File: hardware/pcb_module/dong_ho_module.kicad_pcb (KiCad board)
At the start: 2 copper layers, 50 x 62 mm, 36 parts, among them J1 Motor rung 1027, J2 Pogo sạc (cái, nam châm), J3 Pin LiPo 603040 (JST PH2.0), J4 Dây sang BAT+/BAT- của XIAO, J5 Nút SOS, J6 Dây RA -> vít thép mép vỏ, Q1 AO3400A, U1 XIAO nRF52840 Sense, U2 MAX30102 (module tím), U3 CJMCU-30205, U4 AD8232 (module), U5 GC9A01 1.28in

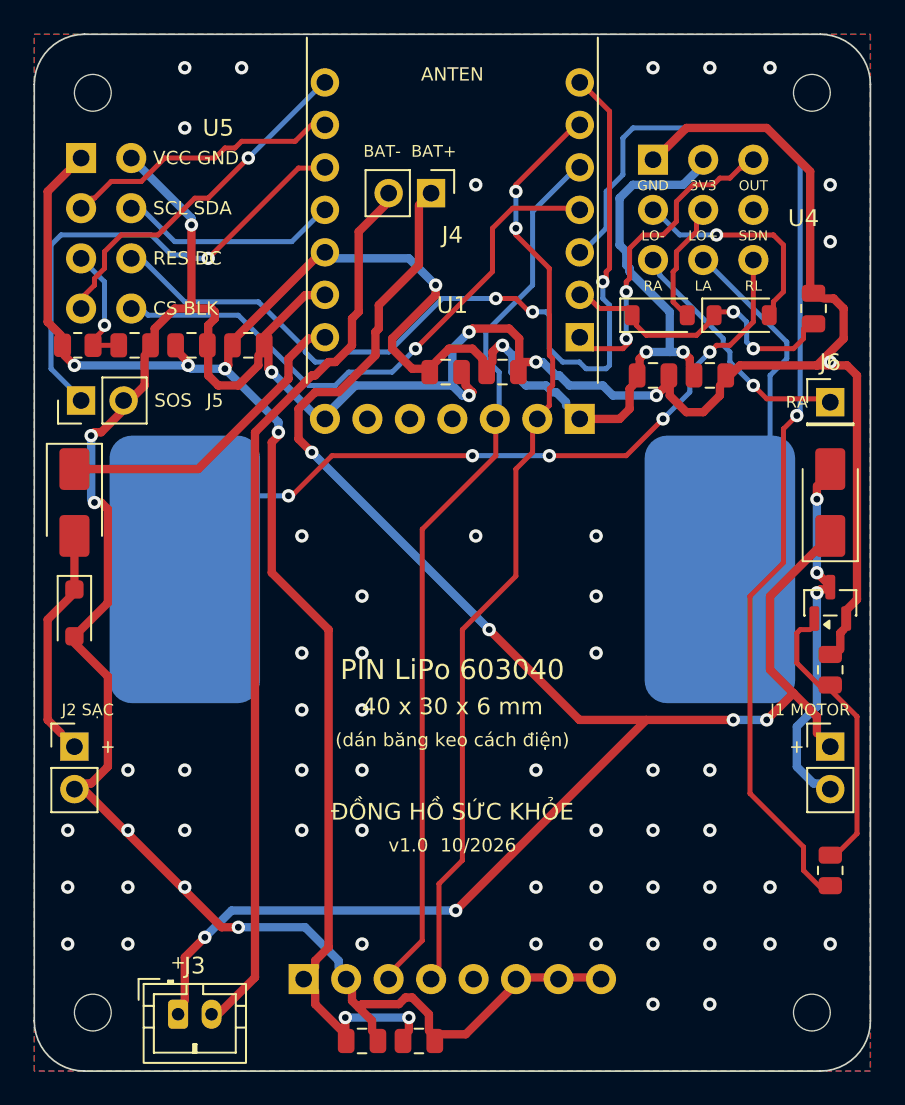
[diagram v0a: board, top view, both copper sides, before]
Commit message: PCB module 1.1: dựng lại bằng KiCad 10 với MAX30102 2x4
- Chạy lại gen_fp/gen_sch/gen_pcb trên KiCad 10.0.7, thêm footprint Module_MAX30102_2x4.
- U2 đổi góc 180 -> 0 (vẫn lật mặt dưới) để chân khớp module thật:
  VIN (28,81; 24,92) ... INT (21,19; 35,08).
- D4 (TVS SMA) dời xuống y 35,4 để courtyard không chồng D5.
- Chữ chân U2 trên lụa 0,6/0,1 mm cho đúng quy tắc lụa.
- ERC 0 lỗi 0 cảnh báo; DRC 0 vi phạm, 0 chưa nối, khớp sơ đồ 0 lỗi.
- Xuất lại PDF, BOM, gerber + khoan, zip và ảnh 3D hai mặt.

Co-Authored-By: Claude Opus 5.5 <noreply@anthropic.com>
Claude-Session: https://claude.ai/code/session_016xjgaR8Q12uTCt4QMw8J44
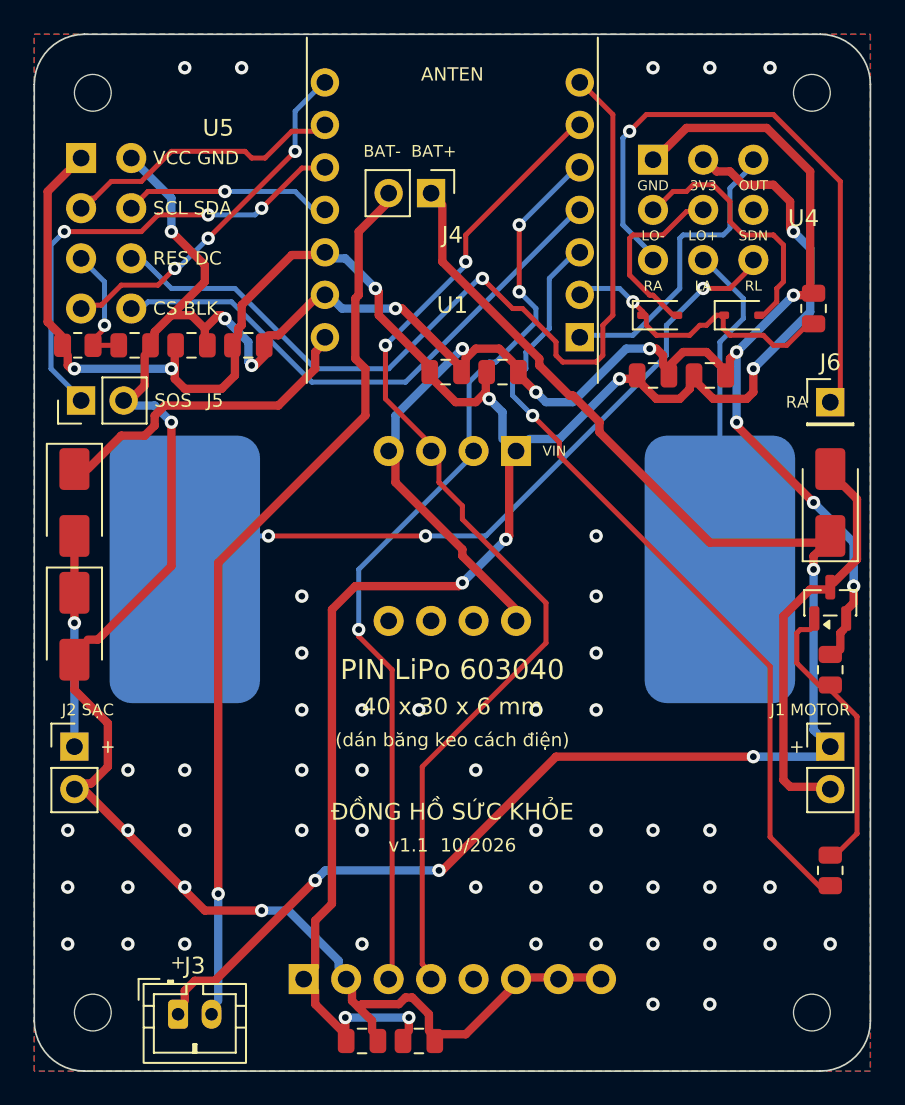
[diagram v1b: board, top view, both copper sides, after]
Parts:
- D2, D3: value 1N4148W -> 1N4148WS; footprint Diode_SMD:D_SOD-123 -> Diode_SMD:D_SOD-323
- D4: value SMF5.0A -> SMAJ5.0A; footprint Diode_SMD:D_SOD-123F -> Diode_SMD:D_SMA
- U2: value MAX30102 (module tím) -> MAX30102 (module 2x4); footprint DoAnModule:Module_MAX30102_1x7 -> DoAnModule:Module_MAX30102_2x4
- moved U2 10.3 mm to (125.0, 130.0), turned to 0 degrees
- moved D4 0.80 mm to (102.4, 135.4)
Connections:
- U2 pad 2: /I2C_SCL -> /I2C_SDA
- U2 pad 3: /I2C_SDA -> /I2C_SCL
- U2 pad 4: unconnected-(U2-INT-Pad4) -> GND
- U2 pad 5: unconnected-(U2-IRD-Pad5) -> GND
- U2 pad 7: GND -> unconnected-(U2-IRD-Pad7)
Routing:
- net /ECG_RA: track 13.3 -> 35.0 mm
- net /MOTOR_EN: track 65.3 -> 46.6 mm
- net /VBAT+: track 104.4 -> 88.5 mm, vias 6 -> 4
- net /I2C_SCL: track 53.3 -> 59.9 mm
- net GND: track 173.3 -> 179.6 mm, vias 63 -> 64
- net +3V3: track 125.0 -> 129.0 mm, vias 10 -> 11
- net /LO_P: track 6.23 -> 10.1 mm
- net /MOTOR_N: track 19.4 -> 22.1 mm, vias 3 -> 0
- net /LO_N: track 11.9 -> 14.5 mm, vias 1 -> 0
- net /VCHG: track 10.9 -> 8.40 mm, vias 0 -> 1
- net /I2C_SDA: track 50.7 -> 53.0 mm, vias 0 -> 3
- net /TFT_BLK: track 33.1 -> 31.5 mm, vias 1 -> 0
- net /ECG_OUT: track 17.6 -> 16.4 mm, vias 2 -> 0
- net /SOS_BTN: track 27.8 -> 26.6 mm, vias 1 -> 3
- net /ECG_LOD: track 15.1 -> 16.2 mm, vias 2 -> 1
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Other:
- board text added: "VIN"
- board text added: "v1.1 10/2026"
- board text removed: "v1.0 10/2026"

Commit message: PCB 1.2: áp tiêu chuẩn xưởng, DRC 0 lỗi, xuất lại Gerber
- Chạy cong_cu/ap_quy_tac_xuong.py trên KiCad 10.0.7: 58 pad xuyên lỗ, 101 via,
  2 vùng phủ GND, 50 chữ lụa, 106 nét lụa.
- Lỗ khoan PTH chỉ còn 0,3 (via), 0,8 (JST) và 1,0 mm (header), pad = lỗ + 0,6 mm;
  via 0,3 / 0,9 mm trên cả F.Cu và B.Cu; phủ đồng GND cách 0,65 mm, thermal 0,5 mm.
  Lỗ bắt vít H1-H4 giữ 2,2 mm không mạ.
- Sửa script: làm tròn khi đổi mm (0,3 + 0,6 bị cắt còn 0,899999 mm làm DRC báo
  202 lỗi via) và đặt cỡ via theo từng lớp (API KiCad 10, hết hộp Debug Alert).
- Dời chữ lụa "RA" cạnh J6 sang trái 0,6 mm cho khỏi chồng viền J6.
- ERC 0 lỗi 0 cảnh báo; DRC 0 lỗi, 0 chưa nối, khớp sơ đồ 0 lỗi; còn 6 cảnh báo
  lib_footprint_mismatch J1-J6 (cố ý nới pad).
- Xuất lại PDF, gerber + khoan, zip và ảnh 3D hai mặt; README ghi lệnh xuất đủ lớp.

Co-Authored-By: Claude Opus 5.5 <noreply@anthropic.com>
Claude-Session: https://claude.ai/code/session_01DtVKYLjz9b4xdEphcSQTzb
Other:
- board text added: "v1.2 10/2026"
- board text removed: "v1.1 10/2026"

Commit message: PCB 1.3: vùng pin 45 mm, chuyển D1/Q1/R1/R2 xuống mặt dưới
- Pin thật đo được 45 x 30 x 5,5 mm (tính cả mạch bảo vệ), dài hơn vùng 40 mm của bản 1.2.
  Vùng pin mặt trên nới tới mép phải (x 5-50 mm); khung pin trên User.Comments/F.Fab và
  chữ lụa đổi thành 45 x 30 x 5.5 mm (PCM ->), nhãn v1.3.
- D1 (SS14), Q1 (AO3400A), R1, R2 chuyển xuống mặt dưới, vào khoảng trống dưới điện cực E1,
  cạnh J1 (cách E1 >= 1 mm). Mặt trên vùng x 145-150 không còn linh kiện dán, chỉ còn pad J1.
- Đi lại dây motor: MOTOR_N, MOTOR_G nối ở mặt dưới; VBAT+ từ XIAO xuống J1 ở mặt trên;
  MOTOR_EN qua 1 via; thêm 2 via GND. Sơ đồ nguyên lý và lưới nối không đổi.
- Script cong_cu/v13_doi_day_phai.py (chạy 1 lần trên bản 1.2), rồi ap_quy_tac_xuong.py.
- ERC 0 lỗi 0 cảnh báo; DRC 0 lỗi, 0 chưa nối, khớp sơ đồ 0 lỗi; còn 6 cảnh báo
  lib_footprint_mismatch J1-J6 như cũ.
- Xuất lại PDF, gerber + khoan, zip, ảnh 3D hai mặt; README ghi pin hàn thẳng vào J3,
  hàn dây motor từ mặt dưới và hàn 4 linh kiện mặt dưới trước.

Co-Authored-By: Claude Opus 5.5 <noreply@anthropic.com>
Claude-Session: https://claude.ai/code/session_01DtVKYLjz9b4xdEphcSQTzb
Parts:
- D1, Q1, R1, R2: moved to B.Cu
- moved D1 16.6 mm to (144.4, 144.3), turned to -90 degrees
- moved Q1 16.4 mm to (144.4, 150.1)
- moved R2 15.5 mm to (147.9, 153.5), turned to 0 degrees
- moved R1 1.08 mm to (147.9, 151.0), turned to 180 degrees
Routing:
- net /MOTOR_N: track 22.1 -> 6.40 mm
- net GND: track 179.6 -> 167.1 mm, vias 64 -> 60
- net /MOTOR_G: track 15.3 -> 4.09 mm
- net /MOTOR_EN: track 46.6 -> 51.0 mm, vias 1 -> 2
- net /VBAT+: track 88.5 -> 92.5 mm, vias 4 -> 3
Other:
- board text added: "45 x 30 x 5.5 mm (PCM →)"
- board text added: "v1.3 10/2026"
- board text removed: "40 x 30 x 6 mm"
- board text removed: "v1.2 10/2026"

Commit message: PCB 1.3: đầu PCM của pin quay sang trái (chỉ đổi lụa)
- Chữ lụa F.Silkscreen "(PCM →)" đổi thành "(← PCM)": mạch bảo vệ của pin nằm ở mép trái,
  sát J3 (dây pin chỉ cần ~5 mm), không đè lên mối hàn J1 (VBAT+/MOTOR_N) ở mép phải.
- Không đổi đồng, lỗ khoan hay mask; F_Cu, B_Cu và file khoan chỉ khác ngày tạo.
- README: đặt pin đầu PCM về mép trái; cắt sát chân U2 và J1 ở mặt trên, dán Kapton,
  lót mút ~1 mm dưới pin.
- DRC 0 lỗi, 0 chưa nối, khớp sơ đồ 0 lỗi; còn 6 cảnh báo lib_footprint_mismatch J1-J6.
- Xuất lại gerber/, gerber_dong_ho_module.zip và pcb_mat_tren.png.

Co-Authored-By: Claude Opus 5.5 <noreply@anthropic.com>
Claude-Session: https://claude.ai/code/session_01DtVKYLjz9b4xdEphcSQTzb
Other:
- board text added: "45 x 30 x 5.5 mm (← PCM)"
- board text removed: "45 x 30 x 5.5 mm (PCM →)"
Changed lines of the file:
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@@
 		)
 	)
-	(gr_text "45 x 30 x 5.5 mm  (PCM →)"
+	(gr_text "45 x 30 x 5.5 mm  (← PCM)"
 		(at 125 140.2 0)
 		(layer "F.SilkS")
